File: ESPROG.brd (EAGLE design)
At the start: 30 x 20 mm, 20 parts, among them IC1 CP2104, J1 USB-C, J2 M06RA, Q1 MMDT3904

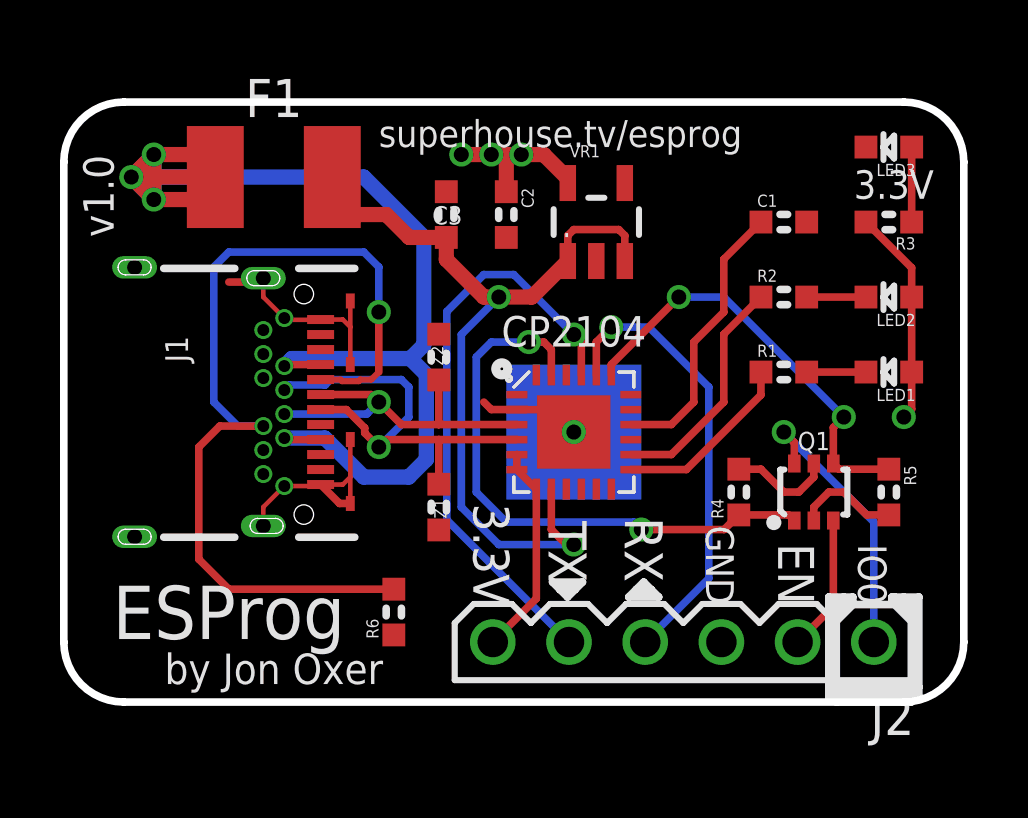
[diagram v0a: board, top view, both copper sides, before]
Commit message: Replaced CP2104 with CP2102N for v1.1 release
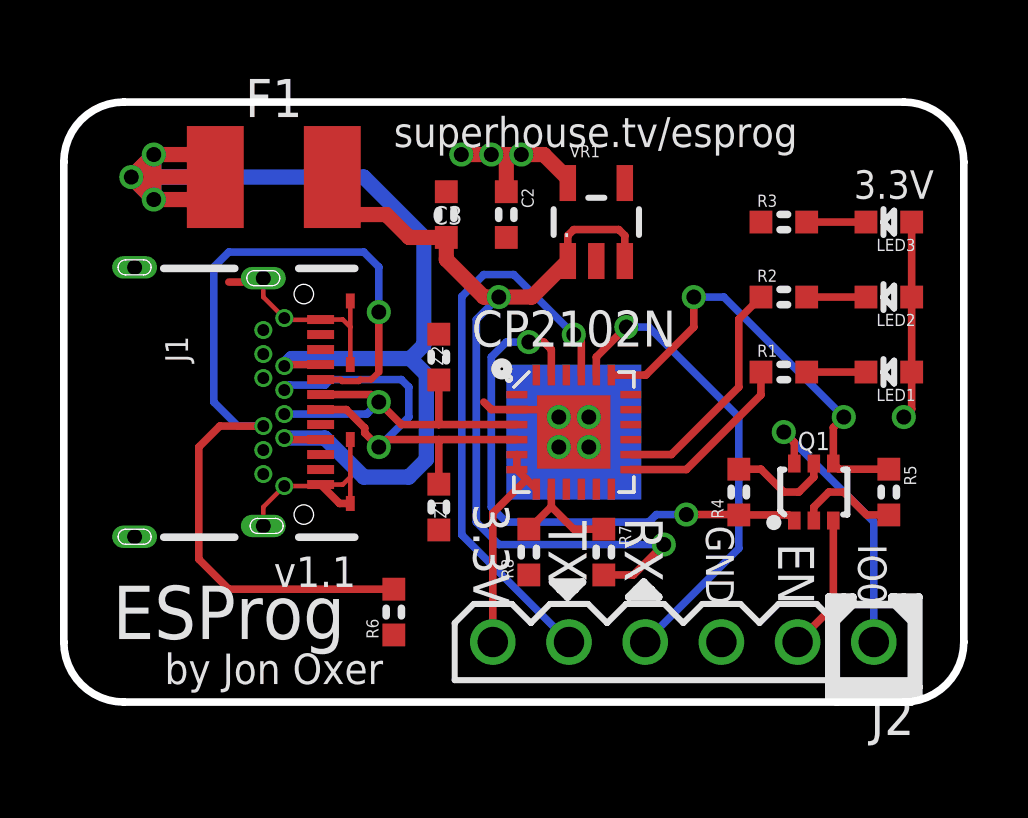
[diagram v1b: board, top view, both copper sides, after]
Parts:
- removed C1: 4.7uF, SuperHouse-DiscreteSemi:C0603
- added R7: 22.1K, SuperHouse-DiscreteSemi:R0603
- added R8: 47.5K, SuperHouse-DiscreteSemi:R0603
- C2: value 1uF -> 4.7uF
- IC1: value CP2104 -> CP2102N-A01-GQFN24
- moved R3 3.50 mm to (24.0, 16.0), turned to 0 degrees
- moved LED3 2.50 mm to (27.5, 16.0)
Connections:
- net 3.3V: now also LED3.A; no longer R3.2
- net 5V: now also R7.2; no longer IC1.8
- net GND: now also R3.1, R8.1; no longer C1.2, LED3.C
- net N$5: now also LED3.C, R3.2; no longer LED3.A, R3.1
- net N$6: now also IC1.8, R7.1, R8.2; no longer C1.1, IC1.16
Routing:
- net N$6: track 9.34 -> 3.71 mm
- net 5V: track 28.7 -> 31.4 mm
- net DTR: track 19.6 -> 18.7 mm
- net N$10: track 15.3 -> 15.8 mm
- net N$5: track 2.50 -> 1.98 mm
- net GND: track 17.9 -> 18.2 mm, vias 1 -> 4
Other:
- board text added: "CP2102N"
- board text added: "v1.1"
- board text removed: "CP2104"
- board text removed: "v1.0"

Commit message: Split CC1 and CC2 on USB connector
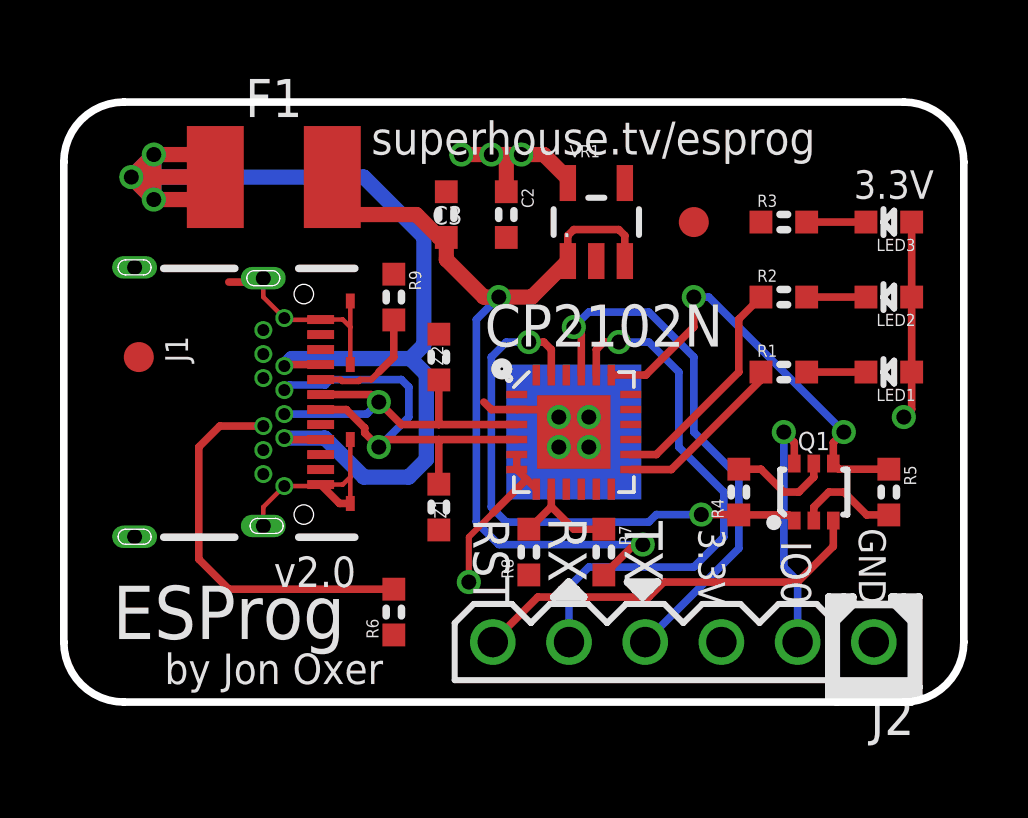
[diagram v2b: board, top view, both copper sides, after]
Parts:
- added FID1, FID2: FIDUCIAL1X2.5, freetronics:FIDUCIAL-1X2.5
- added R9: 5.1K, SuperHouse-DiscreteSemi:R0603
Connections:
- removed net N$10: IC1.20, J2.4
- new net RXI: IC1.20, J2.5
- new net TXO: IC1.21, J2.4
- net 3.3V: now also J2.3; no longer J2.6
- net EN: now also J2.6; no longer J2.2
- net GND: now also J2.1, R9.1; no longer J2.3
- net GPIO0: now also J2.2; no longer J2.1
- net N$67: now also R9.2; no longer J1.B5, R6.2
- net N$9: now also J1.B5, R6.2; no longer IC1.21, J2.5
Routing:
- net N$67: track 31.1 -> 4.03 mm, vias 1 -> 0
- net TXO: track 0.00 -> 17.9 mm, vias 0 -> 1
- net RXI: track 0.00 -> 17.9 mm, vias 0 -> 1
- net N$10: track 15.8 -> 0.00 mm, vias 1 -> 0
- net EN: track 4.54 -> 13.5 mm
- net N$9: track 19.3 -> 13.1 mm, vias 1 -> 0
- net 3.3V: track 19.2 -> 17.5 mm, vias 4 -> 5
- net 5V: track 31.4 -> 30.0 mm
- net GPIO0: track 9.44 -> 8.39 mm
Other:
- board text added: "RST"
- board text added: "v2.0"
- board text removed: "EN"
- board text removed: "v1.1"

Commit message: Major revision of header pinout
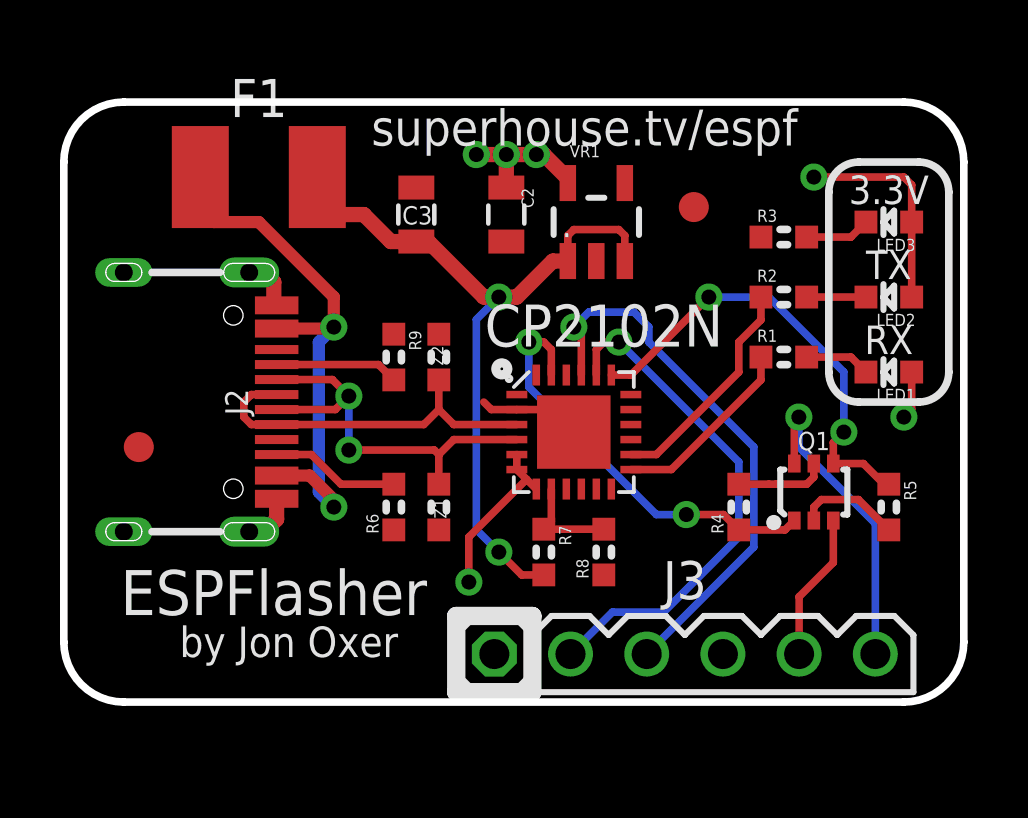
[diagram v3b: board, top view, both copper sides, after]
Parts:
- removed J1: USB-C, SuperHouse-Connectors:USB-C-U52A
- added J3: ESP-PROG-1X6-2.54-PINS-RA, SuperHouse-ESP-Prog:1X6-2.54-PINS-RA
- C2: value 4.7uF -> 10uF; device SuperHouse-DiscreteSemi:C0603 -> SuperHouse-DiscreteSemi:C0805
- C3: value 1uF -> 10uF; device SuperHouse-DiscreteSemi:C0603 -> SuperHouse-DiscreteSemi:C0805
- J2: value M06RA -> USB-C-16P-16P; device SuperHouse-Connectors:1X06RA -> SuperHouse-Connectors:USB-C-16P
- LED1: value GREEN -> YELLOW
- LED2: value YELLOW -> GREEN
- moved J2 26.2 mm to (2.00, 10.0), turned to 270 degrees
- moved R6 3.50 mm to (11.0, 6.50)
- moved FID1 3.00 mm to (2.50, 8.50)
- moved R8 2.50 mm to (18.0, 5.00)
- moved R7 2.00 mm to (16.0, 5.00)
- moved R9 2.00 mm to (11.0, 11.5)
- moved C3 1.00 mm to (11.8, 16.2)
- moved F1 0.50 mm to (6.50, 17.5)
- moved FID2 0.50 mm to (21.0, 16.5)
- moved R1 0.50 mm to (24.0, 11.5)
- moved R3 0.50 mm to (24.0, 15.5)
- moved R4 0.50 mm to (22.5, 6.50)
- moved R5 0.50 mm to (27.5, 6.50)
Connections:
- net N$1 renamed TX_LED
- net N$2 renamed RX_LED
- removed net N$67: J1.A5, R9.2
- new net N$10: J2.A5, R9.2
- net 3.3V: now also J3.4; no longer J2.3
- net D+: now also J2.A6, J2.B6; no longer J1.A6, J1.B6
- net D-: now also J2.A7, J2.B7; no longer J1.A7, J1.B7
- net EN: now also J3.5; no longer J2.6
- net GND: now also J2.A12B1, J2.A1B12, J2.FIX1, J2.FIX2, J2.FIX3, J2.FIX4, J3.1; no longer J1.A1, J1.A12, J1.B1, J1.B12, J1.CASE1, J1.CASE2, J1.CASE3, J1.CASE4, J1.FIX1, J1.FIX2, J1.FIX3, J1.FIX4, J2.1
- net GPIO0: now also J3.6; no longer J2.2
- net N$9: now also J2.B5; no longer J1.B5
- net RXI: now also J3.2; no longer J2.5
- net TXO: now also J3.3; no longer J2.4
- net VIN: now also J2.A4B9, J2.A9B4; no longer J1.A4, J1.A9, J1.B4, J1.B9
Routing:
- net VIN: track 46.3 -> 18.5 mm, vias 3 -> 2
- net GND: track 18.2 -> 7.24 mm, vias 4 -> 0
- net N$9: track 13.1 -> 4.31 mm
- net EN: track 13.5 -> 4.92 mm
- net DTR: track 18.7 -> 14.2 mm
- net N$10: track 0.00 -> 4.12 mm
- net 5V: track 30.0 -> 25.9 mm
- net N$67: track 4.03 -> 0.00 mm
- net GPIO0: track 8.39 -> 10.6 mm
- net D-: track 15.6 -> 13.9 mm, vias 1 -> 2
- net 3.3V: track 17.5 -> 19.0 mm, vias 5 -> 6
- net RXI: track 17.9 -> 17.1 mm
- net RTS: track 14.4 -> 15.2 mm
- net D+: track 11.8 -> 12.3 mm, vias 1 -> 0
- net TXO: track 17.9 -> 18.4 mm
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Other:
- board text added: "Copyright 2020 SuperHouse Automation Released under the TAPR Open Hardware License www.tapr.org/OHL"
- board text added: "ESPFlasher"
- board text added: "G"
- board text added: "superhouse.tv/espf"
- board text added: "v3.0"
- board text removed: "Copyright 2019 SuperHouse Automation Released under the TAPR Open Hardware License www.tapr.org/OHL"
- board text removed: "ESProg"
- board text removed: "GND"
- board text removed: "superhouse.tv/esprog"
- board text removed: "v2.0"
